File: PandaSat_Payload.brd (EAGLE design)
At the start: 93.9 x 90.2 mm, 16 parts, among them J1 U.FL, J4 FEMALE 2x3, J5 U.FL, J6 FEMALE 2x3, U1 CH340G, U12 EP2W+, U14 S1216V8, Y1 12MHz

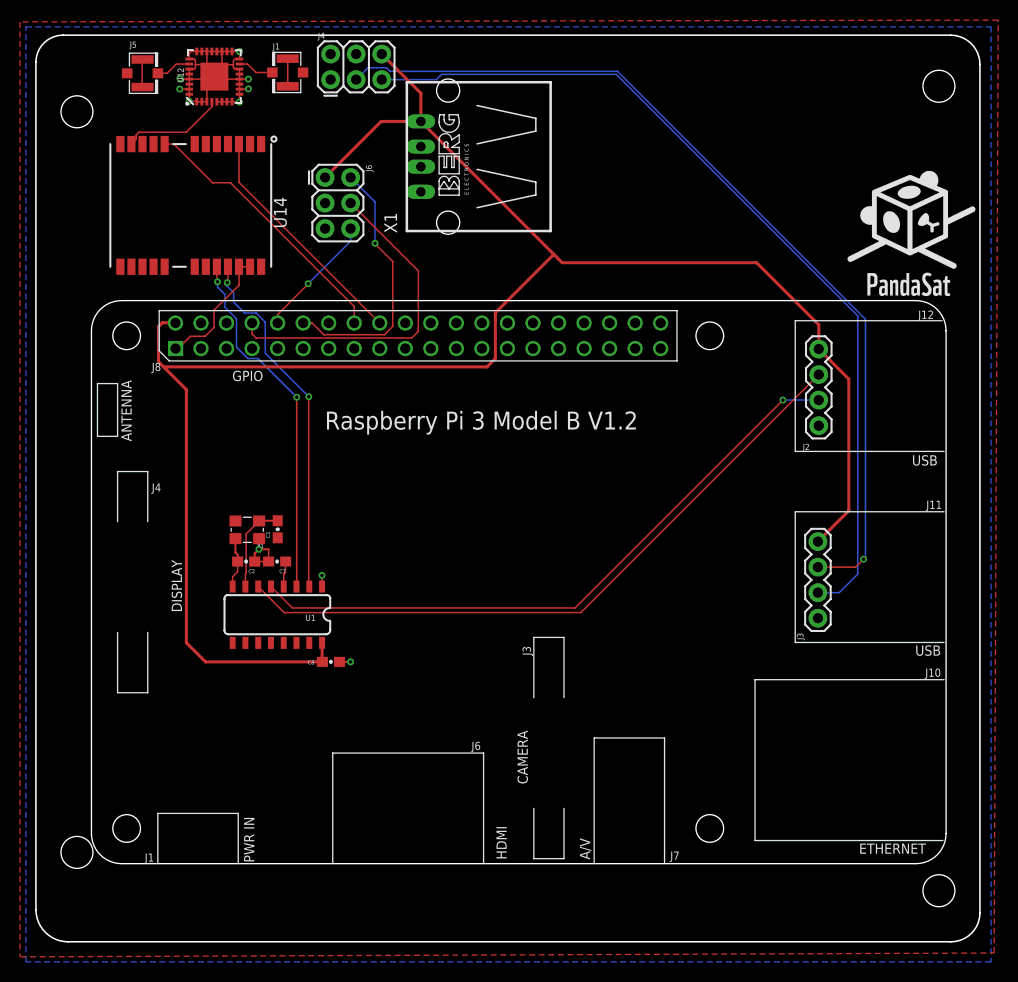
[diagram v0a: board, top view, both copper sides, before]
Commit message: Added new Eagle Files for payload board
-modified pins USB socket
-added 4 pins connector (socket - Pi)
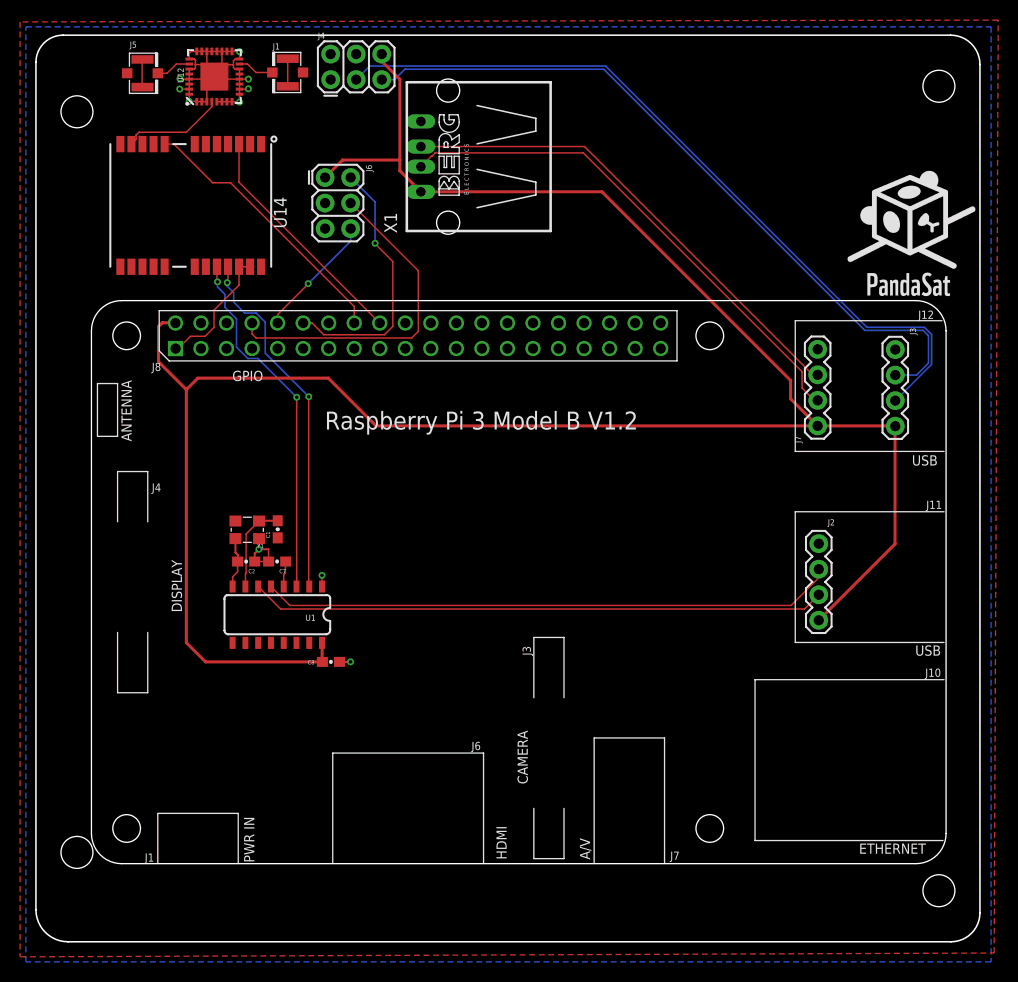
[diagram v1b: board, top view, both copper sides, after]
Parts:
- added J7: (no value), SparkFun-Connectors:1X04
- moved J3 27.8 mm to (85.5, 58.9), turned to 270 degrees
- moved J2 11.7 mm to (77.9, 39.6), turned to 270 degrees
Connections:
- new net N$3: PCB1.P$20
- net D+: now also J7.3, X1.3; no longer X1.2
- net D-: now also J7.2, X1.2; no longer X1.3
- net GND: now also J7.4, PCB1.P$14, PCB1.P$25, PCB1.P$30, PCB1.P$34, PCB1.P$39, PCB1.P$6, X1.4; no longer X1.1
- net VCC5: now also J7.1, X1.1; no longer X1.4
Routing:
- net D-: track 0.00 -> 51.2 mm
- net D+: track 0.00 -> 48.9 mm
- net VCC5: track 189.0 -> 219.8 mm
- net D2+: track 87.9 -> 72.3 mm
- net D2-: track 90.3 -> 76.9 mm, vias 1 -> 0
- net UD-: track 66.6 -> 57.3 mm
- net UD+: track 63.9 -> 57.3 mm, vias 1 -> 0
